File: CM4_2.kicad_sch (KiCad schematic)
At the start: 22 parts, among them J1 Bus_PCI_Express_Mini, J10 PCIE_USB_D-/D+, J11 V_IN1, J12 V_IN2, J17 GPIO_V, J2 USB_A, J20 Controll Connector, J3 USB_HUB, J30 GPIO Connector, J4 USB_B_Micro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

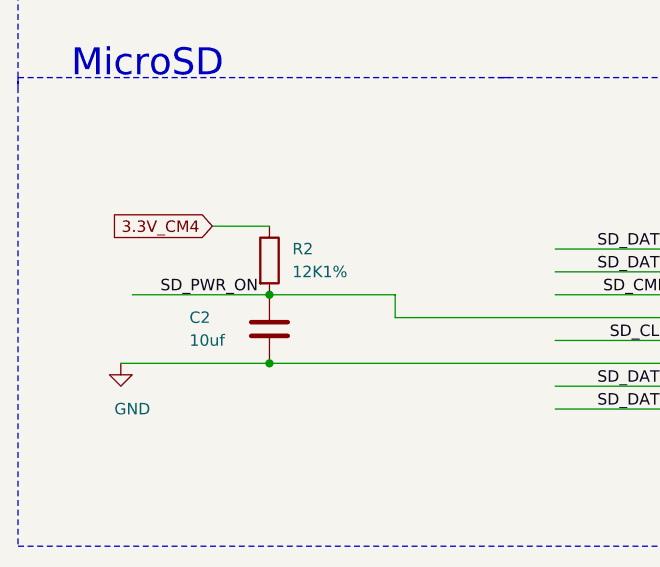
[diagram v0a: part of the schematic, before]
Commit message: Some tracks rerouted, MicroUSB moved
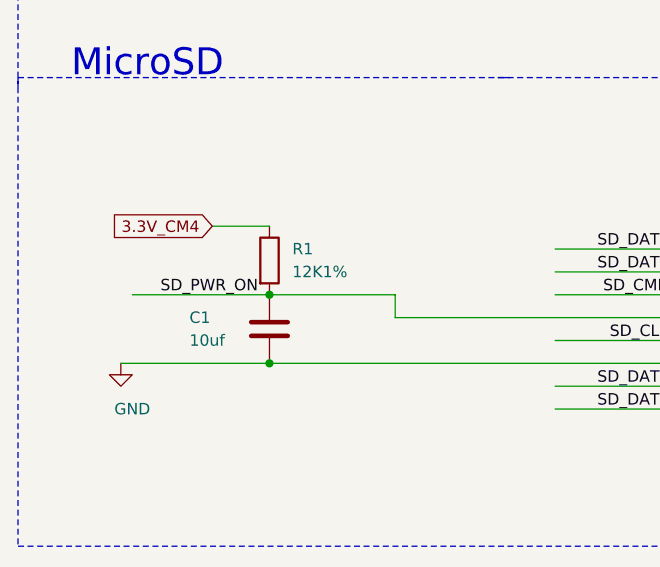
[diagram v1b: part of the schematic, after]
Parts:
- renumbered C2 to C1, R2 to R1
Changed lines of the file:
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@@
   (junction (at 777.24 417.83) (diameter 0.9144) (color 0 0 0 0))
   (junction (at 735.33 327.66) (diameter 0.9144) (color 0 0 0 0))
+  (no_connect (at 650.24 255.27))
+  (no_connect (at 650.24 242.57))
+  (no_connect (at 666.75 403.86))
+  (no_connect (at 650.24 227.33))
+  (no_connect (at 452.12 365.76))
+  (no_connect (at 666.75 393.7))
+  (no_connect (at 650.24 219.71))
+  (no_connect (at 605.79 421.64))
+  (no_connect (at 605.79 393.7))
+  (no_connect (at 513.08 434.34))
+  (no_connect (at 666.75 439.42))
+  (no_connect (at 666.75 378.46))
+  (no_connect (at 650.24 240.03))
+  (no_connect (at 605.79 345.44))
+  (no_connect (at 605.79 378.46))
+  (no_connect (at 650.24 234.95))
+  (no_connect (at 513.08 454.66))
+  (no_connect (at 452.12 444.5))
+  (no_connect (at 605.79 401.32))
+  (no_connect (at 605.79 398.78))
+  (no_connect (at 650.24 252.73))
+  (no_connect (at 605.79 406.4))
+  (no_connect (at 666.75 459.74))
+  (no_connect (at 666.75 452.12))
+  (no_connect (at 650.24 212.09))
+  (no_connect (at 666.75 401.32))
+  (no_connect (at 650.24 229.87))
+  (no_connect (at 650.24 214.63))
+  (no_connect (at 614.68 247.65))
+  (no_connect (at 666.75 444.5))
+  (no_connect (at 666.75 370.84))
+  (no_connect (at 666.75 416.56))
+  (no_connect (at 666.75 429.26))
+  (no_connect (at 666.75 431.8))
+  (no_connect (at 650.24 245.11))
+  (no_connect (at 614.68 240.03))
+  (no_connect (at 650.24 232.41))
+  (no_connect (at 650.24 250.19))
+  (no_connect (at 605.79 408.94))
+  (no_connect (at 605.79 416.56))
+  (no_connect (at 452.12 363.22))
+  (no_connect (at 666.75 363.22))
+  (no_connect (at 666.75 414.02))
+  (no_connect (at 666.75 383.54))
+  (no_connect (at 452.12 441.96))
+  (no_connect (at 605.79 414.02))
+  (no_connect (at 666.75 462.28))
+  (no_connect (at 666.75 447.04))
+  (no_connect (at 605.79 462.28))
+  (no_connect (at 605.79 375.92))
+  (no_connect (at 605.79 347.98))
+  (no_connect (at 513.08 457.2))
+  (no_connect (at 513.08 363.22))
   (no_connect (at 666.75 421.64))
+  (no_connect (at 605.79 424.18))
+  (no_connect (at 513.08 464.82))
+  (no_connect (at 614.68 242.57))
   (no_connect (at 650.24 209.55))
-  (no_connect (at 650.24 250.19))
-  (no_connect (at 666.75 439.42))
-  (no_connect (at 666.75 363.22))
-  (no_connect (at 614.68 242.57))
+  (no_connect (at 666.75 396.24))
+  (no_connect (at 605.79 383.54))
+  (no_connect (at 666.75 368.3))
+  (no_connect (at 513.08 365.76))
+  (no_connect (at 666.75 386.08))
+  (no_connect (at 452.12 360.68))
+  (no_connect (at 666.75 436.88))
+  (no_connect (at 666.75 391.16))
+  (no_connect (at 513.08 360.68))
+  (no_connect (at 614.68 252.73))
+  (no_connect (at 750.57 344.17))
+  (no_connect (at 605.79 386.08))
+  (no_connect (at 666.75 360.68))
+  (no_connect (at 666.75 424.18))
+  (no_connect (at 650.24 222.25))
+  (no_connect (at 650.24 247.65))
+  (no_connect (at 666.75 454.66))
+  (no_connect (at 621.03 554.99))
+  (no_connect (at 605.79 459.74))
   (no_connect (at 666.75 398.78))
   (no_connect (at 605.79 391.16))
-  (no_connect (at 650.24 229.87))
-  (no_connect (at 605.79 401.32))
-  (no_connect (at 605.79 414.02))
-  (no_connect (at 666.75 444.5))
-  (no_connect (at 614.68 247.65))
-  (no_connect (at 666.75 431.8))
-  (no_connect (at 650.24 214.63))
-  (no_connect (at 605.79 462.28))
-  (no_connect (at 605.79 424.18))
-  (no_connect (at 605.79 408.94))
-  (no_connect (at 650.24 240.03))
-  (no_connect (at 666.75 368.3))
-  (no_connect (at 650.24 242.57))
-  (no_connect (at 666.75 452.12))
-  (no_connect (at 666.75 416.56))
-  (no_connect (at 666.75 414.02))
-  (no_connect (at 666.75 436.88))
-  (no_connect (at 666.75 447.04))
-  (no_connect (at 605.79 386.08))
-  (no_connect (at 666.75 454.66))
-  (no_connect (at 666.75 424.18))
-  (no_connect (at 666.75 393.7))
-  (no_connect (at 650.24 232.41))
-  (no_connect (at 605.79 416.56))
-  (no_connect (at 452.12 360.68))
-  (no_connect (at 666.75 391.16))
-  (no_connect (at 513.08 434.34))
-  (no_connect (at 513.08 457.2))
-  (no_connect (at 614.68 252.73))
-  (no_connect (at 650.24 227.33))
-  (no_connect (at 666.75 370.84))
-  (no_connect (at 513.08 363.22))
-  (no_connect (at 605.79 459.74))
-  (no_connect (at 452.12 363.22))
-  (no_connect (at 605.79 378.46))
-  (no_connect (at 650.24 212.09))
-  (no_connect (at 452.12 441.96))
-  (no_connect (at 605.79 393.7))
-  (no_connect (at 666.75 378.46))
   (no_connect (at 666.75 375.92))
-  (no_connect (at 666.75 459.74))
-  (no_connect (at 605.79 406.4))
-  (no_connect (at 452.12 444.5))
-  (no_connect (at 605.79 345.44))
-  (no_connect (at 650.24 222.25))
-  (no_connect (at 605.79 347.98))
-  (no_connect (at 650.24 219.71))
-  (no_connect (at 513.08 464.82))
-  (no_connect (at 513.08 454.66))
-  (no_connect (at 666.75 462.28))
-  (no_connect (at 650.24 247.65))
-  (no_connect (at 666.75 429.26))
-  (no_connect (at 614.68 240.03))
-  (no_connect (at 605.79 421.64))
   (no_connect (at 452.12 436.88))
-  (no_connect (at 666.75 386.08))
-  (no_connect (at 666.75 360.68))
-  (no_connect (at 666.75 401.32))
-  (no_connect (at 666.75 403.86))
-  (no_connect (at 605.79 398.78))
-  (no_connect (at 513.08 360.68))
-  (no_connect (at 750.57 344.17))
-  (no_connect (at 650.24 255.27))
-  (no_connect (at 605.79 375.92))
-  (no_connect (at 621.03 554.99))
-  (no_connect (at 666.75 396.24))
-  (no_connect (at 650.24 234.95))
-  (no_connect (at 666.75 383.54))
-  (no_connect (at 605.79 383.54))
-  (no_connect (at 513.08 365.76))
-  (no_connect (at 650.24 245.11))
-  (no_connect (at 650.24 252.73))
-  (no_connect (at 452.12 365.76))
   (bus_entry (at 681.99 340.36) (size -2.54 2.54)
     (stroke (width 0.1524) (type solid) (color 0 0 0 0))
@@
   (symbol (lib_id "Device:R") (at 402.59 523.24 0) (unit 1)
     (in_bom yes) (on_board yes)
-    (property "Reference" "R2" (id 0) (at 405.13 521.97 0)
+    (property "Reference" "R1" (id 0) (at 405.13 521.97 0)
       (effects (font (size 1.27 1.27)) (justify left))
     )
@@
   (symbol (lib_id "Device:C") (at 402.59 530.86 0) (unit 1)
     (in_bom yes) (on_board yes)
-    (property "Reference" "C2" (id 0) (at 393.7 529.59 0)
+    (property "Reference" "C1" (id 0) (at 393.7 529.59 0)
       (effects (font (size 1.27 1.27)) (justify left))
     )
@@
     )
     (path "/bce73107-69cb-4bc3-a49f-c97225a7d2b6"
-      (reference "C2") (unit 1) (value "10uf") (footprint "Capacitor_SMD:C_1206_3216Metric")
+      (reference "C1") (unit 1) (value "10uf") (footprint "Capacitor_SMD:C_1206_3216Metric")
     )
     (path "/923b803d-0d2b-4396-8811-39e27a4ca584"
@@
     )
     (path "/d9ebbbc3-0a49-4db6-a972-28e730105cd4"
-      (reference "R2") (unit 1) (value "12K1%") (footprint "Resistor_SMD:R_1206_3216Metric")
-    )
-  )
+      (reference "R1") (unit 1) (value "12K1%") (footprint "Resistor_SMD:R_1206_3216Metric")
+    )
+  )

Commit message: v1.01
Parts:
- removed J30: GPIO Connector, Connector_PinHeader_2.54mm:PinHeader_1x06_P2.54mm_Vertical, symbol Connector:Conn_01x06_Female
- removed J41: GND, Connector_PinHeader_2.54mm:PinHeader_1x01_P2.54mm_Vertical, symbol Connector_Generic:Conn_01x01
- added J30: Conn_01x07_Female, Connector_PinSocket_2.54mm:PinSocket_1x07_P2.54mm_Vertical, symbol Connector:Conn_01x07_Female
- J17: footprint Connector_PinHeader_2.54mm:PinHeader_1x03_P2.54mm_Vertical -> Connector_PinHeader_2.54mm:PinHeader_1x03_P2.54mm_Vertical_SMD_Pin1Right
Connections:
- net 1.8V_CM4: now also J17.3 (Pin_3); no longer J17.1 (Pin_1)
- net 3.3V_CM4: now also J17.1 (Pin_1); no longer J17.2 (Pin_2)
- net GND: now also J30.7 (Pin_7)
- net GPIO12: now also J30.4 (Pin_4)
- net GPIO14: now also J30.6 (Pin_6)
- net GPIO15: now also J30.5 (Pin_5)
- net GPIO2: now also J30.1 (Pin_1)
- net GPIO3: now also J30.2 (Pin_2)
- net GPIO4: now also J30.3 (Pin_3)
- net GPIO_VREF: now also J17.2 (Pin_2); no longer J17.3 (Pin_3)
